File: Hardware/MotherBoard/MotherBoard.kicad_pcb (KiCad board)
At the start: 2 copper layers, 145 x 160 mm, 54 parts, among them J1 POWER, J10 I/O_PWR, J11 RDY_PULLUP, J12 NMI_PULLUP, J13 USB_OTG, J14 IRQ0_PULLUP, J2 I/O0, J3 ISA00, J4 ISA10, J5 I/O1, J6 EXTRN_CLCK, J7 ISA01, J8 ISA11, J9 Conn_02x02_Odd_Even, SW1 RESET_SW, SW2 ON_OFF, U1 AMS1117-5.0, U10 74HC245, U11 74HC245, U12 74HC245, U13 74HC541, U14 74HC541, U2 AT28C256, U3 WD65C22, U4 AS6C62256, U5 WD65C02, U6 74HC148, U7 74HC574, U8 ATF16V8B, U9 74HC245, X1 ACO-1MHz

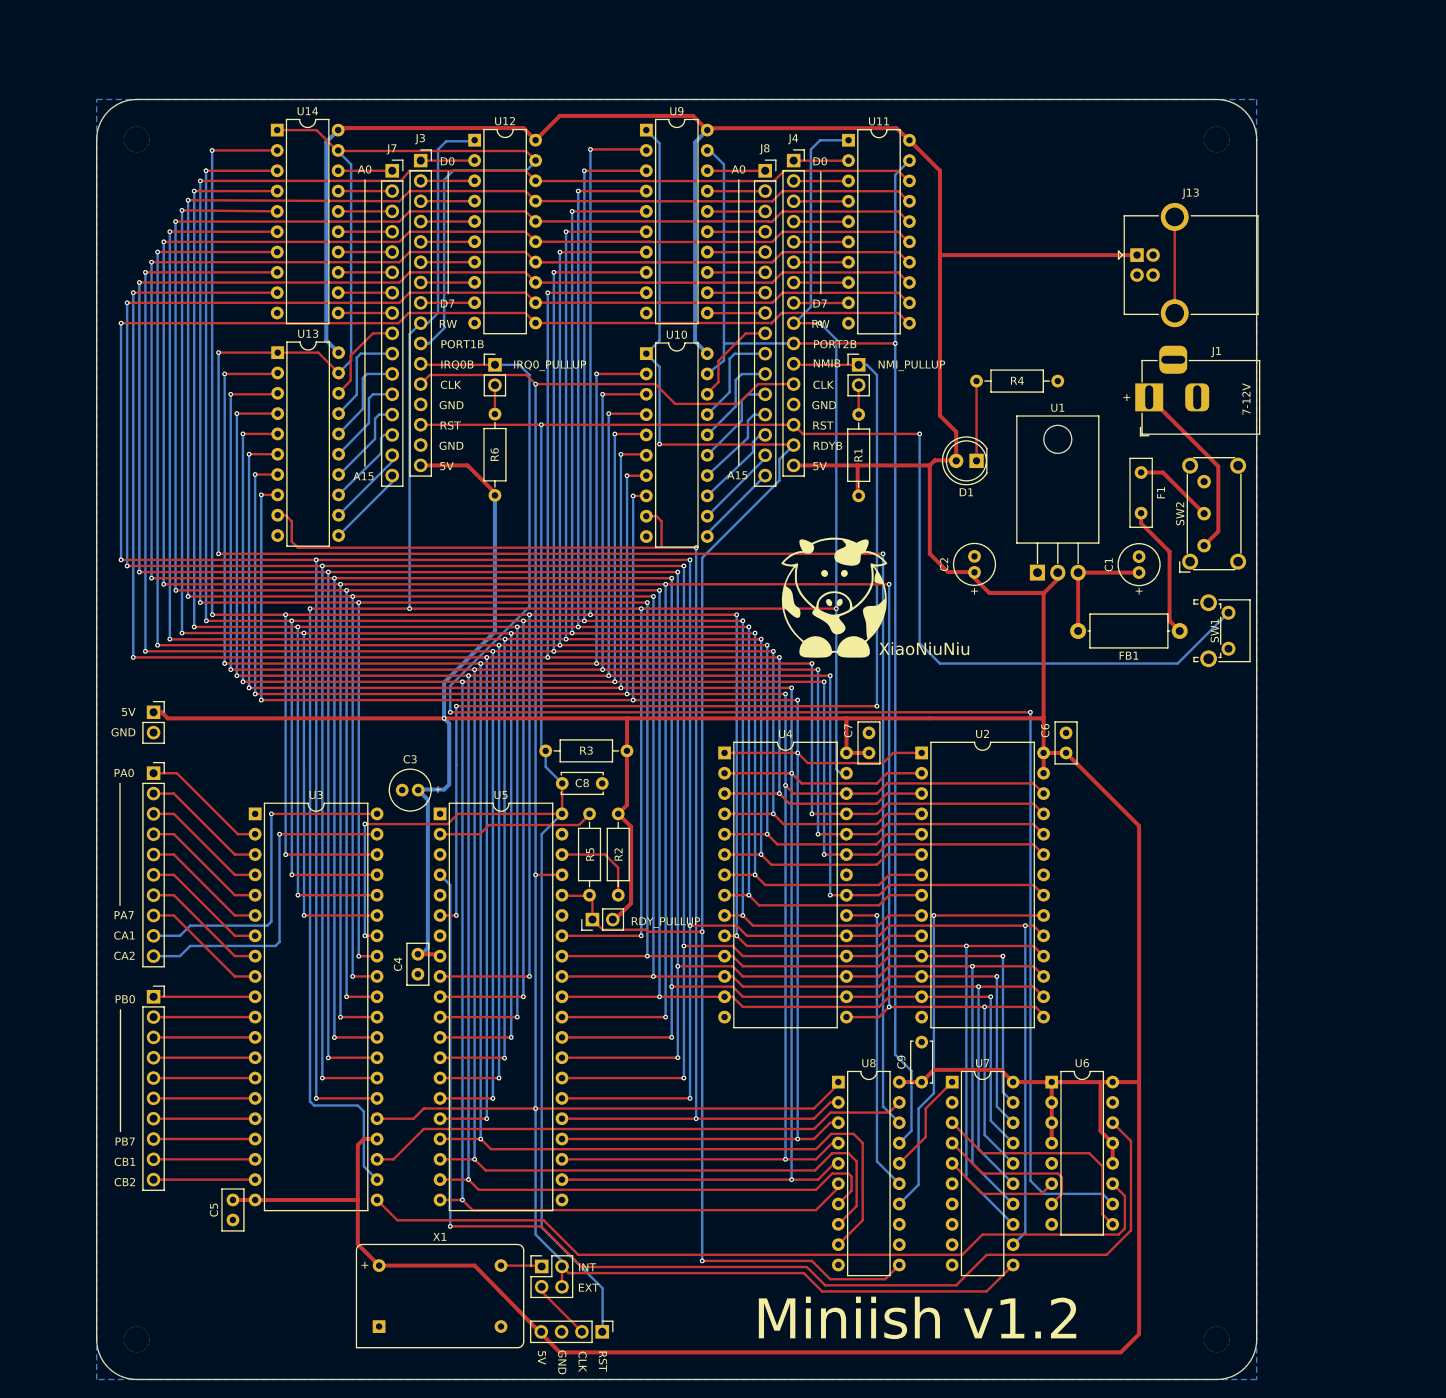
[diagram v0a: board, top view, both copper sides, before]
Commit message: New PLD logic, VGA, DMA ...
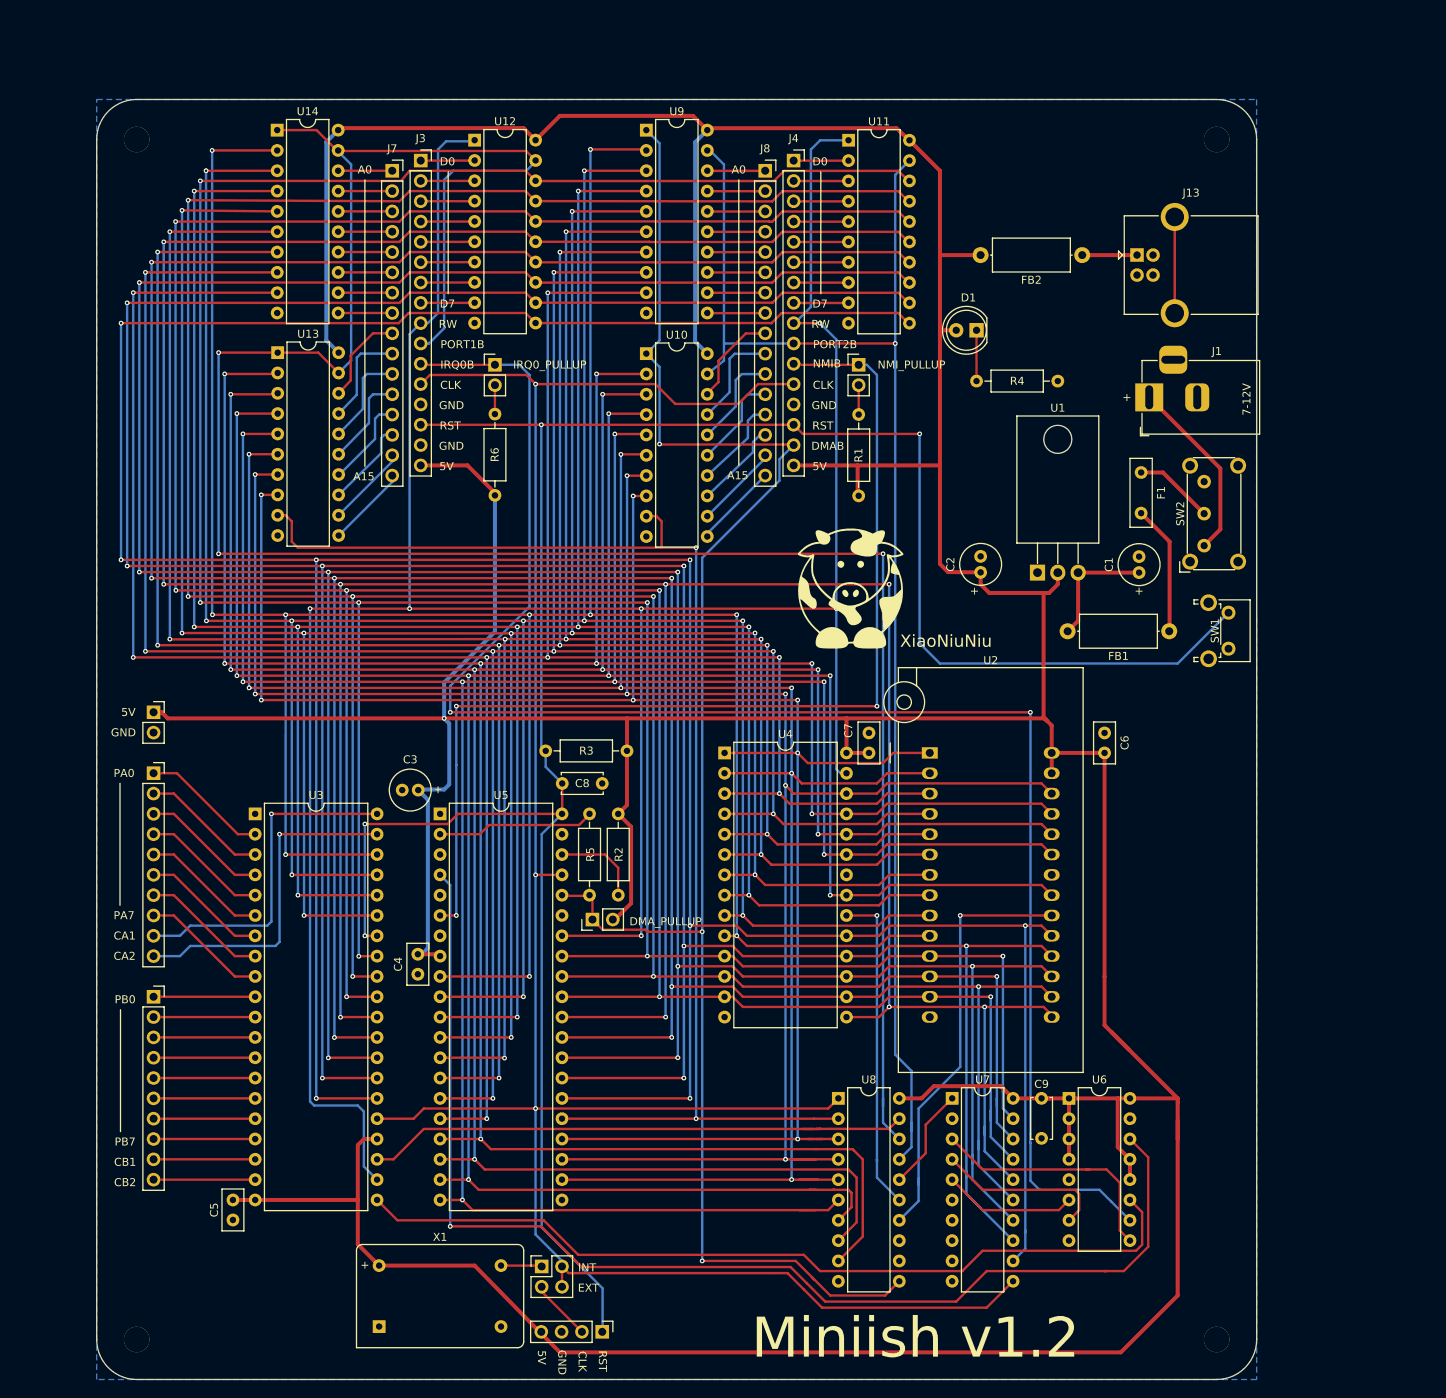
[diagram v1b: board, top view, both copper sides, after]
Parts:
- added FB2: 100 @ 100MHz, Inductor_THT:L_Axial_L9.5mm_D4.0mm_P12.70mm_Horizontal_Fastron_SMCC, F.Cu at (146.3, 44.5)
- J11: value RDY_PULLUP -> DMA_PULLUP
- U2: footprint Package_DIP:DIP-28_W15.24mm -> Socket:DIP_Socket-28_W11.9_W12.7_W15.24_W17.78_W18.5_3M_228-1277-00-0602J
- moved D1 16.3 mm to (133.1, 53.8)
- moved C9 15.1 mm to (141.2, 149.9), turned to -90 degrees
- moved C6 4.81 mm to (149.1, 106.7)
- moved U6 2.96 mm to (144.7, 149.9)
- moved XiaoNiuNiu 2.33 mm to (117.3, 86.1)
- moved U7 2.03 mm to (130.0, 149.9)
- moved U8 2.03 mm to (115.8, 149.9)
- moved FB1 1.31 mm to (157.2, 91.5)
- moved U2 1.02 mm to (127.3, 106.7)
- moved C2 0.77 mm to (133.6, 84.1)
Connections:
- net /CLOCK renamed CLOCK
- net IRQ0B renamed /IRQ0B
- net RDYB renamed DMAB
- net no_connect_125 renamed no_connect_126
- J13 pad 1: +5V -> Net-(FB2-Pad1)
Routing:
- net Net-(FB2-Pad1): track 0.00 -> 6.86 mm
- net /D5: track 423.1 -> 427.2 mm
- net /D4: track 409.6 -> 413.6 mm
- net /D3: track 453.9 -> 457.9 mm
- net /D6: track 436.1 -> 439.9 mm
- net /A13: track 253.5 -> 257.2 mm
- net Net-(D1-Pad1): track 9.92 -> 6.35 mm
- net /D7: track 445.8 -> 449.1 mm
- net /D2: track 379.8 -> 383.1 mm
- net /IRQB: track 149.9 -> 153.1 mm
- net /PORT2B: track 175.9 -> 179.0 mm
- net /PORT1B: track 293.6 -> 296.7 mm
- net /D1: track 372.4 -> 375.5 mm
- net /IRQ0B: track 202.8 -> 205.8 mm
- net /IRQ1B: track 103.9 -> 106.9 mm
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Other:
- board text added: "DMAB"
- board text removed: "RDYB"

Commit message: Fix
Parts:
- removed J7: ISA01, Connector_PinSocket_2.54mm:PinSocket_1x16_P2.54mm_Vertical
- removed J8: ISA11, Connector_PinSocket_2.54mm:PinSocket_1x16_P2.54mm_Vertical
- added F2: 500mA, Resistor_THT:R_Box_L8.4mm_W2.5mm_P5.08mm, F.Cu at (141.6, 62.4)
- added R7: 10K, Resistor_THT:R_Axial_DIN0207_L6.3mm_D2.5mm_P10.16mm_Horizontal, F.Cu at (79.3, 104.6)
- J3: value ISA00 -> ISA1; footprint Connector_PinSocket_2.54mm:PinSocket_1x16_P2.54mm_Vertical -> Connector_PinSocket_2.54mm:PinSocket_2x16_P2.54mm_Vertical
- J4: value ISA10 -> ISA0; footprint Connector_PinSocket_2.54mm:PinSocket_1x16_P2.54mm_Vertical -> Connector_PinSocket_2.54mm:PinSocket_2x16_P2.54mm_Vertical
- U8: value ATF16V8B -> ATF22V10B; footprint Package_DIP:DIP-20_W7.62mm -> Package_DIP:DIP-24_W7.62mm
- moved XiaoNiuNiu 50.6 mm to (158.6, 115.3), turned to -90 degrees
- moved J4 46.8 mm to (63.5, 32.9)
- moved J3 46.6 mm to (110.2, 32.9)
- moved U1 35.5 mm to (137.4, 48.8)
- moved C1 29.7 mm to (146.2, 55.3)
- moved C2 28.8 mm to (133.9, 55.3)
- moved FB2 27.5 mm to (141.6, 71.6), turned to -90 degrees
- moved FB1 22.1 mm to (147.7, 71.6), turned to -90 degrees
- moved C9 14.3 mm to (127.0, 150.0)
- moved F1 11.0 mm to (147.7, 62.4)
- moved D1 10.5 mm to (134.7, 64.2)
- moved R4 9.32 mm to (134.8, 69.4), turned to -90 degrees
- moved R3 1.51 mm to (89.5, 107.9)
- moved C8 0.70 mm to (81.3, 111.2)
- moved U6 0.43 mm to (144.3, 150.1)
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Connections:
- net no_connect_126 renamed no_connect_129
- C2 pad 1: +5V -> Net-(C2-Pad1)
- FB2 pad 1: Net-(FB2-Pad1) -> Net-(F2-Pad2)
- FB2 pad 2: +5V -> Net-(C2-Pad1)
- J1 pad 1: Net-(J1-Pad1) -> Net-(F1-Pad1)
- J11 pad 1: DMAB -> /DMAB
- J11 pad 2: +5V -> Net-(J11-Pad2)
- J12 pad 1: NMIB -> /NMIB
- J13 pad 1: Net-(FB2-Pad1) -> Net-(F2-Pad1)
- J3 pad 10: /PORT1B -> /PORT2B
- J3 pad 11: /IRQ0B -> /NMIB
- J3 pad 15: GND -> /DMAB
- J4 pad 10: /PORT2B -> /PORT1B
- J4 pad 11: NMIB -> /IRQ0B
- J4 pad 15: DMAB -> GND
- R5 pad 2: DMAB -> /DMAB
- SW2 pad 1: Net-(J1-Pad1) -> Net-(C2-Pad1)
- SW2 pad 2: Net-(F1-Pad1) -> +5V
- U1 pad 2: +5V -> Net-(C2-Pad1)
- U10 pad 1: DMAB -> /DMAB
- U10 pad 11: Net-(J8-Pad16) -> Net-(J3-Pad32)
- U10 pad 12: Net-(J8-Pad15) -> Net-(J3-Pad31)
- U10 pad 13: Net-(J8-Pad14) -> Net-(J3-Pad30)
- U10 pad 14: Net-(J8-Pad13) -> Net-(J3-Pad29)
- U10 pad 15: Net-(J8-Pad12) -> Net-(J3-Pad28)
- U10 pad 16: Net-(J8-Pad11) -> Net-(J3-Pad27)
- U10 pad 17: Net-(J8-Pad10) -> Net-(J3-Pad26)
- U10 pad 18: Net-(J8-Pad9) -> Net-(J3-Pad25)
- U11 pad 1: /RW -> /DMARW
- U11 pad 2: Net-(J4-Pad1) -> Net-(J3-Pad1)
- U11 pad 3: Net-(J4-Pad2) -> Net-(J3-Pad2)
- U11 pad 4: Net-(J4-Pad3) -> Net-(J3-Pad3)
- U11 pad 5: Net-(J4-Pad4) -> Net-(J3-Pad4)
- U11 pad 6: Net-(J4-Pad5) -> Net-(J3-Pad5)
- U11 pad 7: Net-(J4-Pad6) -> Net-(J3-Pad6)
- U11 pad 8: Net-(J4-Pad7) -> Net-(J3-Pad7)
- U11 pad 9: Net-(J4-Pad8) -> Net-(J3-Pad8)
- U12 pad 2: Net-(J3-Pad1) -> Net-(J4-Pad1)
- U12 pad 3: Net-(J3-Pad2) -> Net-(J4-Pad2)
- U12 pad 4: Net-(J3-Pad3) -> Net-(J4-Pad3)
- U12 pad 5: Net-(J3-Pad4) -> Net-(J4-Pad4)
- U12 pad 6: Net-(J3-Pad5) -> Net-(J4-Pad5)
- U12 pad 7: Net-(J3-Pad6) -> Net-(J4-Pad6)
- U12 pad 8: Net-(J3-Pad7) -> Net-(J4-Pad7)
- U12 pad 9: Net-(J3-Pad8) -> Net-(J4-Pad8)
- U13 pad 11: Net-(J7-Pad16) -> Net-(J4-Pad32)
- U13 pad 12: Net-(J7-Pad15) -> Net-(J4-Pad31)
- U13 pad 13: Net-(J7-Pad14) -> Net-(J4-Pad30)
- U13 pad 14: Net-(J7-Pad13) -> Net-(J4-Pad29)
- U13 pad 15: Net-(J7-Pad12) -> Net-(J4-Pad28)
- U13 pad 16: Net-(J7-Pad11) -> Net-(J4-Pad27)
- U13 pad 17: Net-(J7-Pad10) -> Net-(J4-Pad26)
- U13 pad 18: Net-(J7-Pad9) -> Net-(J4-Pad25)
- U14 pad 11: Net-(J7-Pad8) -> Net-(J4-Pad24)
- U14 pad 12: Net-(J7-Pad7) -> Net-(J4-Pad23)
- U14 pad 13: Net-(J7-Pad6) -> Net-(J4-Pad22)
- U14 pad 14: Net-(J7-Pad5) -> Net-(J4-Pad21)
- U14 pad 15: Net-(J7-Pad4) -> Net-(J4-Pad20)
- U14 pad 16: Net-(J7-Pad3) -> Net-(J4-Pad19)
- U14 pad 17: Net-(J7-Pad2) -> Net-(J4-Pad18)
- U14 pad 18: Net-(J7-Pad1) -> Net-(J4-Pad17)
- U5 pad 36: DMAB -> /DMAB
- U5 pad 6: NMIB -> /NMIB
- U6 pad 10: /IRQ0B -> +5V
- U6 pad 11: /IRQ1B -> +5V
- U6 pad 3: +5V -> /IRQ1B
- U6 pad 4: +5V -> /IRQ0B
- U8 pad 10: GND -> /RW
- U8 pad 11: DMAB -> /DMAB
- U8 pad 12: (no net) -> GND
- U8 pad 13: (no net) -> GND
- U8 pad 14: /ROMCSB -> (no net)
- U8 pad 15: /RAMCSB -> (no net)
- U8 pad 16: Net-(U7-Pad1) -> (no net)
- U8 pad 17: /PORT2B -> /DMARW
- U8 pad 18: /PORT1B -> /ROMCSB
- U8 pad 19: /IOCSB -> /RAMCSB
- U8 pad 20: +5V -> Net-(U7-Pad1)
- U9 pad 1: DMAB -> /DMAB
- U9 pad 11: Net-(J8-Pad8) -> Net-(J3-Pad24)
- U9 pad 12: Net-(J8-Pad7) -> Net-(J3-Pad23)
- U9 pad 13: Net-(J8-Pad6) -> Net-(J3-Pad22)
- U9 pad 14: Net-(J8-Pad5) -> Net-(J3-Pad21)
- U9 pad 15: Net-(J8-Pad4) -> Net-(J3-Pad20)
- U9 pad 16: Net-(J8-Pad3) -> Net-(J3-Pad19)
- U9 pad 17: Net-(J8-Pad2) -> Net-(J3-Pad18)
- U9 pad 18: Net-(J8-Pad1) -> Net-(J3-Pad17)
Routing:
- net DMAB: track 212.6 -> 0.00 mm, vias 3 -> 0
- net /DMAB: track 0.00 -> 205.7 mm, vias 0 -> 3
- net /DMARW: track 0.00 -> 145.8 mm
- net NMIB: track 133.0 -> 0.00 mm, vias 3 -> 0
- net /NMIB: track 0.00 -> 128.1 mm, vias 0 -> 3
- net Net-(C2-Pad1): track 0.00 -> 64.6 mm
- net /D3: track 457.9 -> 399.8 mm, vias 9 -> 7
- net /RW: track 347.3 -> 393.4 mm
- net Net-(C1-Pad1): track 15.5 -> 43.6 mm
- net Net-(F2-Pad1): track 0.00 -> 25.3 mm
- net Net-(J11-Pad2): track 0.00 -> 24.9 mm
- net /A15: track 167.2 -> 191.5 mm, vias 2 -> 5
- net Net-(J1-Pad1): track 23.1 -> 0.00 mm
- net /IRQ0B: track 205.8 -> 192.3 mm
- net Net-(J3-Pad25): track 0.00 -> 12.9 mm
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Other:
- board text added: "Miniish v1.2b"
- board text removed: "Miniish v1.2"
